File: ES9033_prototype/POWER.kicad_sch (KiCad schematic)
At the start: 8 parts, among them U301 TVS1400DRV

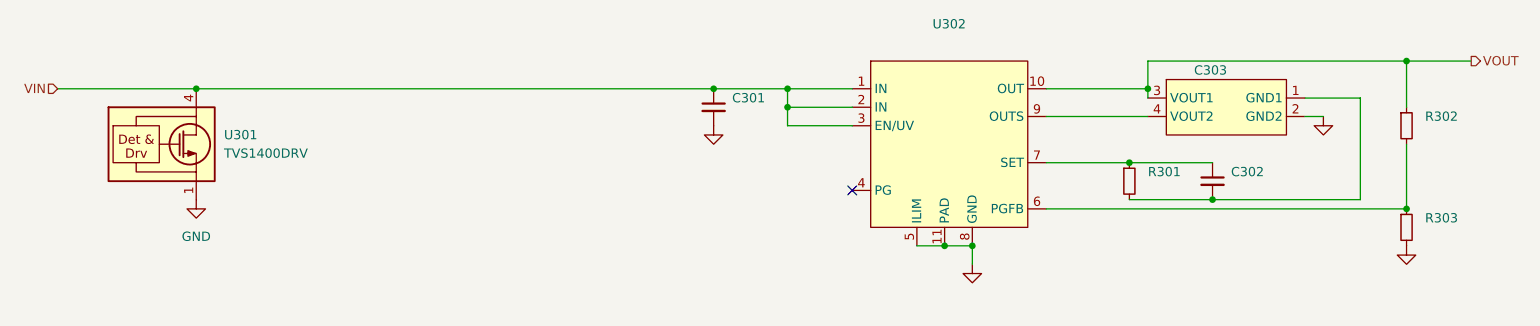
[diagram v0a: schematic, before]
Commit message: removed grounding from mounting holes
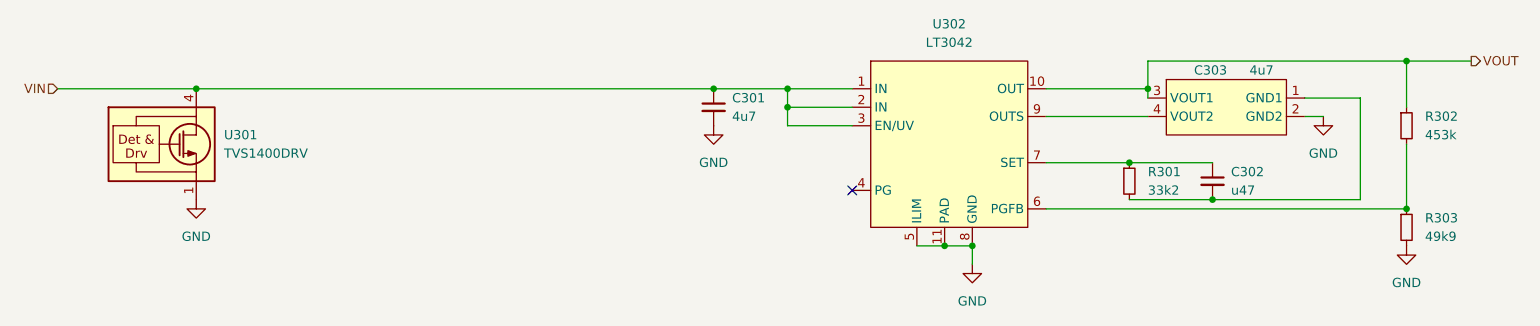
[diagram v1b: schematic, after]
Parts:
- C301: value (none) -> 4u7; footprint (none) -> Capacitor_SMD:C_1206_3216Metric
- C302: value (none) -> u47; footprint (none) -> Capacitor_SMD:C_1206_3216Metric
- C303: value (none) -> 4u7; footprint (none) -> project_lib:1206_split
- R301: value (none) -> 33k2; footprint (none) -> Resistor_SMD:R_0805_2012Metric
- R302: value (none) -> 453k; footprint (none) -> Resistor_SMD:R_0805_2012Metric
- R303: value (none) -> 49k9; footprint (none) -> Resistor_SMD:R_0805_2012Metric
- U302: value (none) -> LT3042; footprint (none) -> Package_DFN_QFN:DFN-10-1EP_3x3mm_P0.5mm_EP1.7x2.5mm
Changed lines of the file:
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@@
       (effects (font (size 1.27 1.27)) (justify left))
     )
-    (property "Value" "" (id 1) (at 190.5 63.5 0)
-      (effects (font (size 1.27 1.27)) (justify left))
-    )
-    (property "Footprint" "" (id 2) (at 187.96 62.23 0)
+    (property "Value" "u47" (id 1) (at 190.5 63.5 0)
+      (effects (font (size 1.27 1.27)) (justify left))
+    )
+    (property "Footprint" "Capacitor_SMD:C_1206_3216Metric" (id 2) (at 187.96 62.23 0)
       (effects (font (size 1.27 1.27)) hide)
     )
@@
       (effects (font (size 1.27 1.27)) (justify left))
     )
-    (property "Value" "" (id 1) (at 217.17 55.8799 0)
-      (effects (font (size 1.27 1.27)) (justify left))
-    )
-    (property "Footprint" "" (id 2) (at 214.63 54.61 0)
+    (property "Value" "453k" (id 1) (at 217.17 55.8799 0)
+      (effects (font (size 1.27 1.27)) (justify left))
+    )
+    (property "Footprint" "Resistor_SMD:R_0805_2012Metric" (id 2) (at 214.63 54.61 0)
       (effects (font (size 1.27 1.27)) hide)
     )
@@
       (effects (font (size 1.27 1.27)) hide)
     )
-    (property "Value" "" (id 1) (at 154.94 78.74 0))
+    (property "Value" "GND" (id 1) (at 154.94 78.74 0))
     (property "Footprint" "" (id 2) (at 154.94 73.66 0)
       (effects (font (size 1.27 1.27)) hide)
@@
       (effects (font (size 1.27 1.27)) hide)
     )
-    (property "Value" "" (id 1) (at 214.63 76.2 0))
+    (property "Value" "GND" (id 1) (at 214.63 76.2 0))
     (property "Footprint" "" (id 2) (at 214.63 71.12 0)
       (effects (font (size 1.27 1.27)) hide)
@@
     (in_bom yes) (on_board yes) (fields_autoplaced)
     (property "Reference" "U302" (id 0) (at 151.765 40.64 0))
-    (property "Value" "" (id 1) (at 151.765 43.18 0))
-    (property "Footprint" "" (id 2) (at 151.13 58.42 0)
+    (property "Value" "LT3042" (id 1) (at 151.765 43.18 0))
+    (property "Footprint" "Package_DFN_QFN:DFN-10-1EP_3x3mm_P0.5mm_EP1.7x2.5mm" (id 2) (at 151.13 58.42 0)
       (effects (font (size 1.27 1.27)) hide)
     )
@@
       (effects (font (size 1.27 1.27)) hide)
     )
-    (property "Value" "" (id 1) (at 119.38 59.69 0))
+    (property "Value" "GND" (id 1) (at 119.38 59.69 0))
     (property "Footprint" "" (id 2) (at 119.38 54.61 0)
       (effects (font (size 1.27 1.27)) hide)
@@
       (effects (font (size 1.27 1.27)) hide)
     )
-    (property "Value" "" (id 1) (at 203.2 58.42 0))
+    (property "Value" "GND" (id 1) (at 203.2 58.42 0))
     (property "Footprint" "" (id 2) (at 203.2 53.34 0)
       (effects (font (size 1.27 1.27)) hide)
@@
       (effects (font (size 1.27 1.27)) (justify left))
     )
-    (property "Value" "" (id 1) (at 121.92 53.3462 0)
-      (effects (font (size 1.27 1.27)) (justify left))
-    )
-    (property "Footprint" "" (id 2) (at 119.38 52.07 0)
+    (property "Value" "4u7" (id 1) (at 121.92 53.3462 0)
+      (effects (font (size 1.27 1.27)) (justify left))
+    )
+    (property "Footprint" "Capacitor_SMD:C_1206_3216Metric" (id 2) (at 119.38 52.07 0)
       (effects (font (size 1.27 1.27)) hide)
     )
@@
       (effects (font (size 1.27 1.27)) (justify left))
     )
-    (property "Value" "" (id 1) (at 217.17 69.8499 0)
-      (effects (font (size 1.27 1.27)) (justify left))
-    )
-    (property "Footprint" "" (id 2) (at 214.63 68.58 0)
+    (property "Value" "49k9" (id 1) (at 217.17 69.8499 0)
+      (effects (font (size 1.27 1.27)) (justify left))
+    )
+    (property "Footprint" "Resistor_SMD:R_0805_2012Metric" (id 2) (at 214.63 68.58 0)
       (effects (font (size 1.27 1.27)) hide)
     )
@@
       (effects (font (size 1.27 1.27)) (justify left))
     )
-    (property "Value" "" (id 1) (at 179.07 63.4999 0)
-      (effects (font (size 1.27 1.27)) (justify left))
-    )
-    (property "Footprint" "" (id 2) (at 176.53 62.23 0)
+    (property "Value" "33k2" (id 1) (at 179.07 63.4999 0)
+      (effects (font (size 1.27 1.27)) (justify left))
+    )
+    (property "Footprint" "Resistor_SMD:R_0805_2012Metric" (id 2) (at 176.53 62.23 0)
       (effects (font (size 1.27 1.27)) hide)
     )
@@
       (effects (font (size 1.27 1.27)) (justify left))
     )
-    (property "Value" "" (id 1) (at 193.04 46.99 0)
-      (effects (font (size 1.27 1.27)) (justify left))
-    )
-    (property "Footprint" "" (id 2) (at 187.325 52.705 90)
-      (effects (font (size 1.27 1.27)) hide)
-    )
+    (property "Value" "4u7" (id 1) (at 193.04 46.99 0)
+      (effects (font (size 1.27 1.27)) (justify left))
+    )
+    (property "Footprint" "project_lib:1206_split" (id 2) (at 187.325 52.705 90)
+      (effects (font (size 1.27 1.27)) hide)
+    )
